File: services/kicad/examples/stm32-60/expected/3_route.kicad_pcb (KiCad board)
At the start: 2 copper layers, 132 x 99 mm, 60 parts, among them J1 5V, U1 STM32F103C8T6, U2 AMS1117-3.3

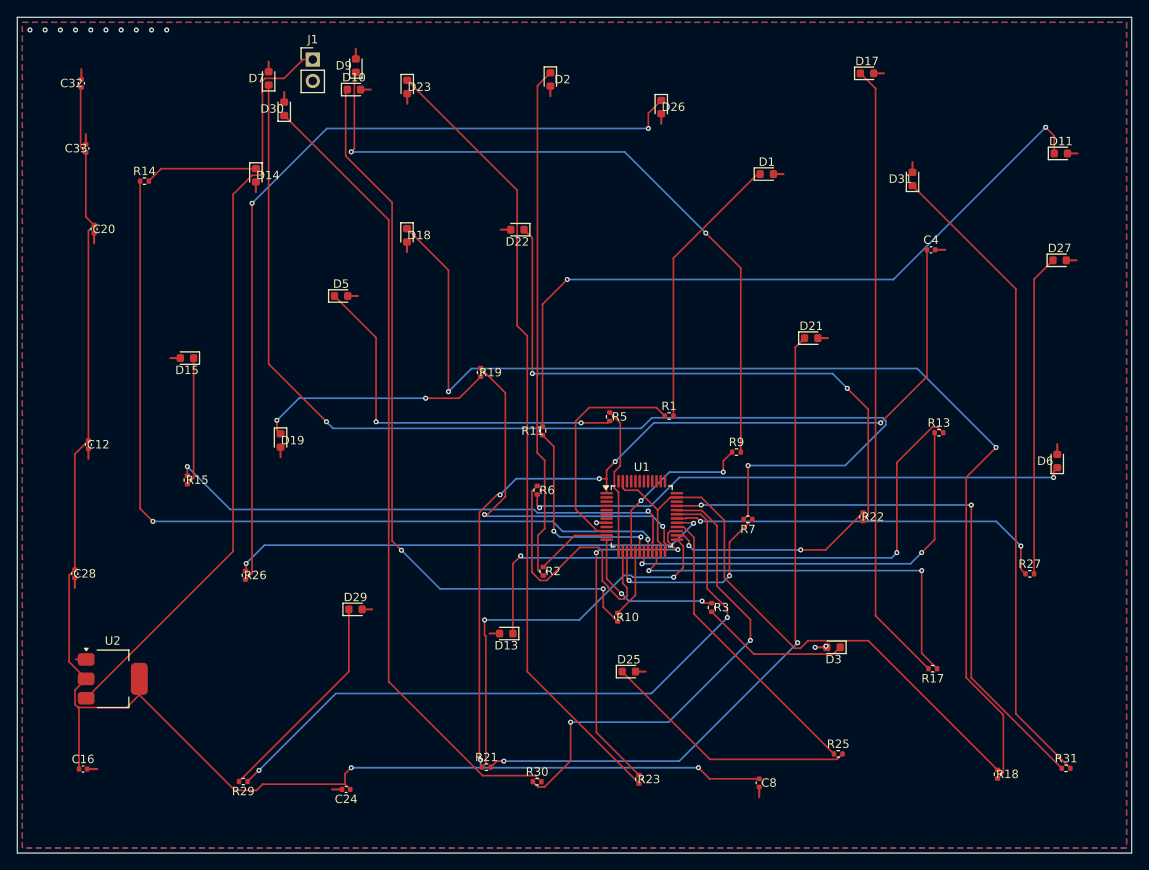
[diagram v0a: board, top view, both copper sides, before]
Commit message: test(examples): references stm32-*/esp32 -- 3_route.kicad_pcb et mesures-routage.json alignes sur les boards livres
Co-Authored-By: Claude Fable 5.1 <noreply@anthropic.com>
Claude-Session: https://claude.ai/code/session_01TnMqm4La2CxQHHB5K8aSSV
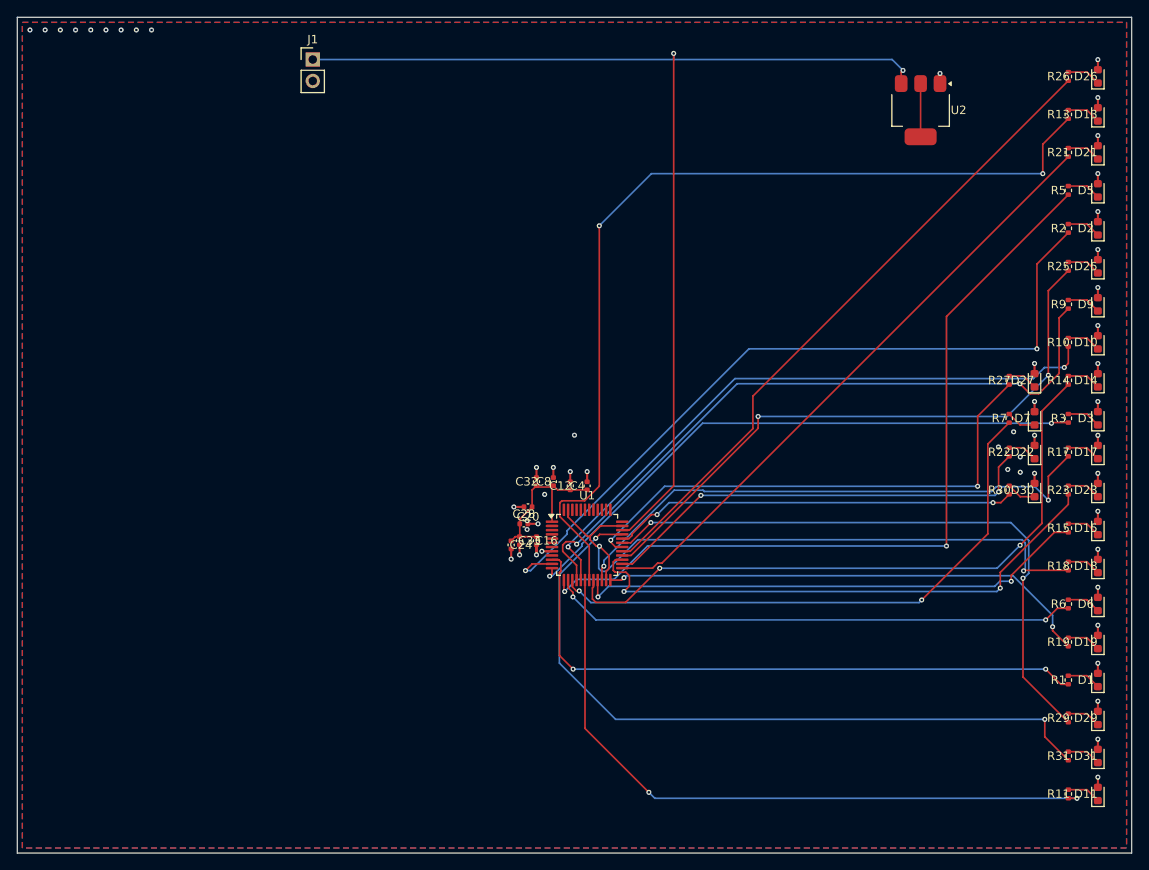
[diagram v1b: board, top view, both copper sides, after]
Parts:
- moved U2 117.0 mm to (189.5, 66.5), turned to -90 degrees
- moved R26 114.0 mm to (207.0, 62.5), turned to 90 degrees
- moved R14 112.0 mm to (207.0, 98.5), turned to 90 degrees
- moved D15 109.8 mm to (210.5, 116.0), turned to 90 degrees
- moved R15 104.5 mm to (207.0, 116.0), turned to 90 degrees
- moved D14 102.7 mm to (210.5, 98.5), turned to 90 degrees
- moved R21 100.3 mm to (207.0, 71.5), turned to 90 degrees
- moved D19 99.7 mm to (210.5, 129.5), turned to 90 degrees
- moved D30 99.7 mm to (203.0, 111.5)
- moved D7 99.3 mm to (203.0, 103.0)
- moved R29 98.0 mm to (207.0, 138.5), turned to 90 degrees
- moved D23 94.7 mm to (210.5, 111.5), turned to 90 degrees
- moved D13 93.2 mm to (210.5, 67.0), turned to 90 degrees
- moved D10 93.1 mm to (210.5, 94.0), turned to 90 degrees
- moved D9 92.3 mm to (210.5, 89.5)
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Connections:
- C12 pad 1: +3.3V -> +3V3
- C16 pad 1: +3.3V -> +3V3
- C20 pad 1: +3.3V -> +3V3
- C24 pad 1: +3.3V -> +3V3
- C28 pad 1: +3.3V -> +3V3
- C32 pad 1: +3.3V -> +3V3
- C33 pad 1: +3.3V -> +3V3
- C4 pad 1: +3.3V -> +3V3
- C8 pad 1: +3.3V -> +3V3
- U1 pad 1: +3.3V -> +3V3
- U1 pad 34: Net-(U1-34) -> VIN
- U2 pad 2: +3.3V -> Net-(U2-2)
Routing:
- net +3.3V: track 282.6 -> 0.00 mm, vias 7 -> 0
- net LED7: track 135.4 -> 3.54 mm, vias 2 -> 0
- net LED18: track 134.0 -> 4.04 mm, vias 2 -> 0
- net LED26: track 99.5 -> 4.04 mm, vias 2 -> 0
- net LED30: track 95.2 -> 3.54 mm
- net LED23: track 94.7 -> 4.04 mm
- net LED10: track 87.8 -> 4.04 mm, vias 2 -> 0
- net LED11: track 86.3 -> 4.04 mm, vias 2 -> 0
- net GPIO2: track 9.06 -> 90.5 mm, vias 0 -> 2
- net LED9: track 83.3 -> 4.04 mm, vias 2 -> 0
- net GPIO5: track 17.5 -> 96.5 mm, vias 0 -> 2
- net LED21: track 79.1 -> 4.04 mm, vias 2 -> 0
- net LED31: track 76.8 -> 4.04 mm
- net LED17: track 73.9 -> 4.04 mm
- net LED22: track 72.5 -> 3.54 mm, vias 2 -> 0
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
